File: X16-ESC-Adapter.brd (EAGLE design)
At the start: 101.6 x 41.2 mm, 0 parts

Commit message: Included the needed parts
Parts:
- added J1: CONN_1824750000, X16-ESC-Adapter:CONN3_1824750000_WED
- added U$1: CONN_BACKPLANE_ESC_ADAPTER, X16-ESC-Adapter:CONN_BACKPLANE_ESC_ADAPTER
- added U$2: CONN_JST_8_PIN, X16-ESC-Adapter:JST_8_PIN
- added U$3: LUMENIER, X16-ESC-Adapter:LUMENIER

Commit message: Curren tprogress on schem
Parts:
- removed J1: CONN_1824750000, X16-ESC-Adapter:CONN3_1824750000_WED
- removed U$2: CONN_JST_8_PIN, X16-ESC-Adapter:JST_8_PIN
- removed U$3: LUMENIER, X16-ESC-Adapter:LUMENIER
- added D1: GREEN, SparkFun-LED:LED-0603
- added ESC1, ESC2, ESC3, ESC4: CONN_1824750000, X16-ESC-Adapter:CONN3_1824750000_WED
- added LUMENIER_ESC_PORT: CONN_JST_8_PIN, X16-ESC-Adapter:JST_8_PIN
- added LUMINIER_ESC: LUMENIER, X16-ESC-Adapter:LUMENIER
- added RIZZ: 600, SparkFun-Resistors:0603
- renumbered U$1 to PWR
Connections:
- new net 12V: LUMINIER_ESC.VIN, PWR.12V@10, PWR.12V@11, PWR.12V@12, PWR.12V@3, PWR.12V@4, PWR.12V@5, PWR.12V@6, PWR.12V@7, PWR.12V@8, PWR.12V@9, RIZZ.1
- new net ESC1A: ESC1.1, ESC1.2, LUMINIER_ESC.1
- new net ESC1B: ESC1.3, ESC1.4, LUMINIER_ESC.2
- new net ESC1C: ESC1.5, ESC1.6, LUMINIER_ESC.3
- new net ESC2A: ESC2.1, ESC2.2, LUMINIER_ESC.4
- new net ESC2B: ESC2.3, ESC2.4, LUMINIER_ESC.5
- new net ESC2C: ESC2.5, ESC2.6, LUMINIER_ESC.6
- new net ESC3A: ESC3.5, ESC3.6, LUMINIER_ESC.9
- new net ESC3B: ESC3.3, ESC3.4, LUMINIER_ESC.8
- new net ESC3C: ESC3.1, ESC3.2, LUMINIER_ESC.7
- new net ESC4A: ESC4.5, ESC4.6, LUMINIER_ESC.12
- new net ESC4B: ESC4.3, ESC4.4, LUMINIER_ESC.11
- new net ESC4C: ESC4.1, ESC4.2, LUMINIER_ESC.10
- new net GND: D1.C, LUMENIER_ESC_PORT.2, LUMENIER_ESC_PORT.MECH1, LUMENIER_ESC_PORT.MECH2, LUMINIER_ESC.GND, PWR.GND@1, PWR.GND@10, PWR.GND@2, PWR.GND@3, PWR.GND@4, PWR.GND@5, PWR.GND@6, PWR.GND@7, PWR.GND@8, PWR.GND@9
- new net MTR_1: LUMENIER_ESC_PORT.5, PWR.PWM0
- new net MTR_2: LUMENIER_ESC_PORT.6, PWR.PWM1
- new net MTR_3: LUMENIER_ESC_PORT.7, PWR.PWM2
- new net MTR_4: LUMENIER_ESC_PORT.8, PWR.PWM3
- new net N$1: D1.A, RIZZ.2
- new net N$7: PWR.NC@1, PWR.NC@2, PWR.NC@3, PWR.NC@4, PWR.NC@5, PWR.NC@6
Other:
- board size 101.6 x 41.2 mm -> 101.6 x 41.1 mm

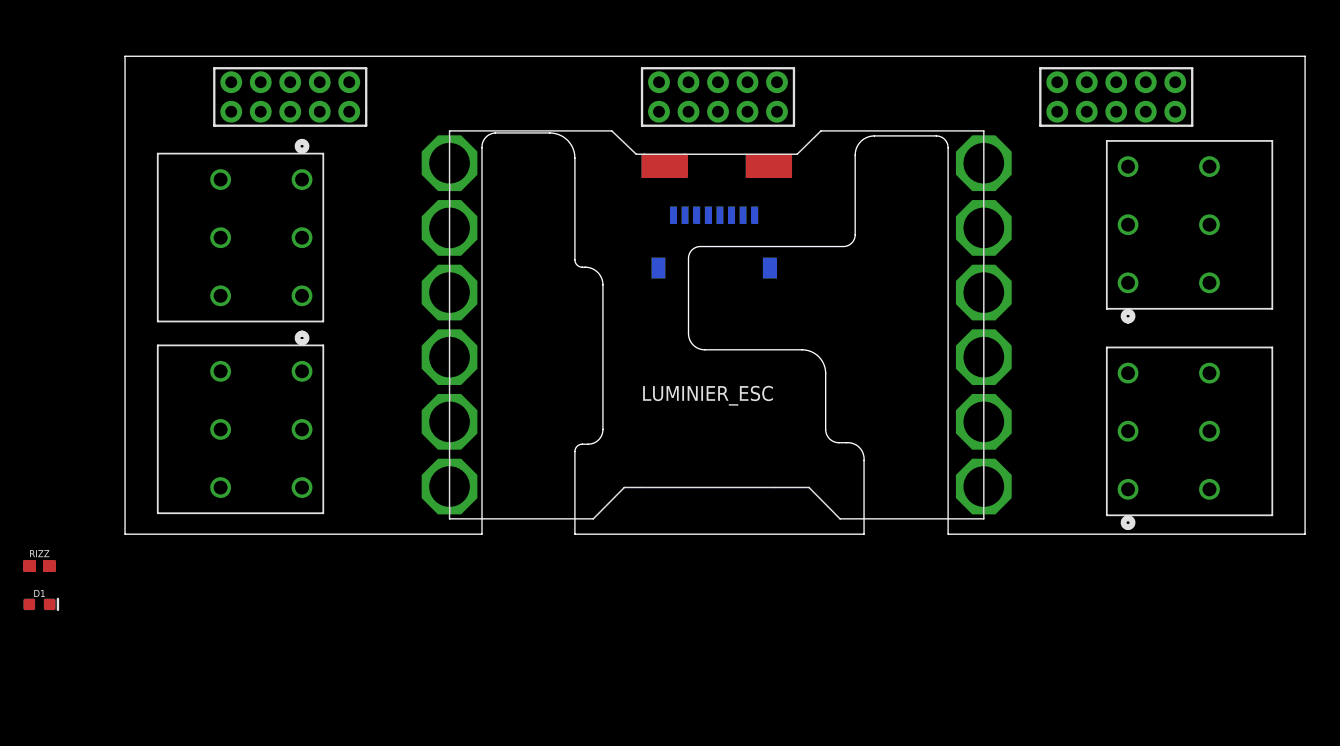
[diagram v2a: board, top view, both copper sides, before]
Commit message: Update X16-ESC-Adapter.brd
10/4/23 - Started Board Circuitry
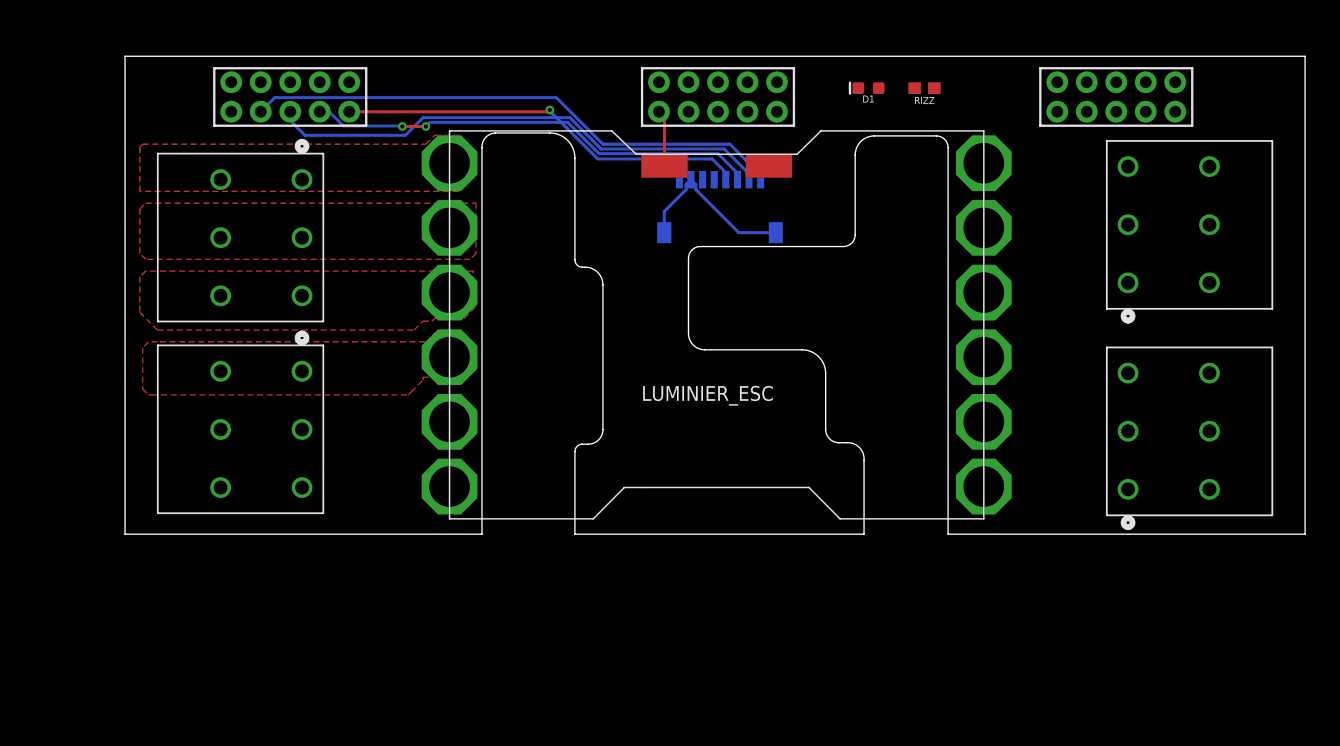
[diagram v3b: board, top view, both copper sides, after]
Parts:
- moved RIZZ 86.6 mm to (68.8, 38.4), turned to 180 degrees
- moved D1 84.1 mm to (64.0, 38.4), turned to 180 degrees
- moved LUMENIER_ESC_PORT 3.09 mm to (46.2, 29.7)
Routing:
- net MTR_4: track 0.00 -> 46.7 mm
- net MTR_3: track 0.00 -> 43.9 mm
- net MTR_2: track 0.00 -> 39.0 mm, vias 0 -> 2
- net MTR_1: track 0.00 -> 35.4 mm, vias 0 -> 1
- net GND: track 0.00 -> 22.6 mm
- added copper zone on layer 1, net ESC1A
- added copper zone on layer 1, net ESC1B
- added copper zone on layer 1, net ESC1C
- added copper zone on layer 1, net ESC2A
- added copper zone on layer 1, net N$2

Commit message: Update X16-ESC-Adapter.brd
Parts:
- moved RIZZ 4.83 mm to (64.0, 38.6)
- moved D1 3.31 mm to (60.7, 38.6)
- moved LUMENIER_ESC_PORT 0.76 mm to (46.2, 30.5)
- moved ESC3 0.51 mm to (86.4, 4.32)
- moved ESC1 0.51 mm to (15.2, 31.0)
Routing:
- net MTR_4: track 46.7 -> 51.3 mm
- net MTR_3: track 43.9 -> 48.3 mm
- net MTR_2: track 39.0 -> 42.2 mm
- net N$1: track 0.00 -> 1.58 mm
- net MTR_1: track 35.4 -> 36.1 mm, vias 1 -> 2
- net GND: track 22.6 -> 23.2 mm
- added copper zone on layer 1, net 12V
- added copper zone on layer 16, net ESC1A
- added copper zone on layer 16, net ESC1B
- added copper zone on layer 16, net ESC1C
- added copper zone on layer 16, net ESC2A
- added copper zone on layer 1, net ESC2B
- added copper zone on layer 16, net ESC2B
- added copper zone on layer 1, net ESC2C
- added copper zone on layer 16, net ESC2C
- added copper zone on layer 1, net ESC3A
- added copper zone on layer 16, net ESC3A
- added copper zone on layer 1, net ESC3B
- added copper zone on layer 16, net ESC3B
- added copper zone on layer 1, net ESC3C
- added copper zone on layer 16, net ESC3C
- added copper zone on layer 1, net ESC4A
- added copper zone on layer 16, net ESC4A
- added copper zone on layer 1, net ESC4B
- added copper zone on layer 16, net ESC4B
- added copper zone on layer 1, net ESC4C
- added copper zone on layer 16, net ESC4C
- added copper zone on layer 1, net GND
- removed copper zone on layer 1, net N$2

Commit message: Finished Layout
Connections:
- removed net N$7: PWR.NC@1, PWR.NC@2, PWR.NC@3, PWR.NC@4, PWR.NC@5, PWR.NC@6
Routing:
- net GND: track 23.2 -> 25.5 mm, vias 0 -> 1
- net MTR_3: track 48.3 -> 50.0 mm

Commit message: First set of changes after alumni design review
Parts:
- removed D1: GREEN, SparkFun-LED:LED-0603
- added HOPE: (no value), led:CHIPLED_0805
- moved LUMENIER_ESC_PORT 37.5 mm to (9.65, 38.6)
- moved RIZZ 3.57 mm to (67.6, 38.4)
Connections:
- net GND: now also HOPE.C; no longer D1.C
- net N$1: now also HOPE.A; no longer D1.A
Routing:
- net MTR_4: track 51.1 -> 0.00 mm
- net MTR_3: track 50.0 -> 0.00 mm
- net MTR_2: track 42.5 -> 0.00 mm, vias 2 -> 0
- net MTR_1: track 35.8 -> 0.00 mm, vias 2 -> 0
- net GND: track 25.5 -> 0.00 mm, vias 1 -> 0
- net N$1: track 1.58 -> 0.00 mm
- added copper zone on layer 16, net GND
- added copper zone on layer 1, net PWR
- removed copper zone on layer 1, net 12V
- removed copper zone on layer 1, net GND
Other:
- outline, holes or cut-outs redrawn

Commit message: Updated (11/4)
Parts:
- removed LUMENIER_ESC_PORT: CONN_JST_8_PIN, X16-ESC-Adapter:JST_8_PIN
- added J1: BM08B-SRSS-TB(LF)(SN), X16-ESC-Adapter:JST_BM08B-SRSS-TB(LF)(SN)
- moved RIZZ 0.72 mm to (68.1, 38.9)
- moved HOPE 0.72 mm to (62.7, 38.9)
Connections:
- net GND: now also J1.S1, J1.S2; no longer LUMENIER_ESC_PORT.2, LUMENIER_ESC_PORT.MECH1, LUMENIER_ESC_PORT.MECH2
- net MTR_1: now also J1.1; no longer LUMENIER_ESC_PORT.5
- net MTR_2: now also J1.2; no longer LUMENIER_ESC_PORT.6
- net MTR_3: now also J1.3; no longer LUMENIER_ESC_PORT.7
- net MTR_4: now also J1.4; no longer LUMENIER_ESC_PORT.8
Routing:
- net MTR_4: track 0.00 -> 20.7 mm
- net MTR_3: track 0.00 -> 16.4 mm
- net MTR_2: track 0.00 -> 11.8 mm
- net MTR_1: track 0.00 -> 6.69 mm
- net GND: track 0.00 -> 5.55 mm
- net N$1: track 0.00 -> 3.43 mm
- added copper zone on layer 1, net 12V
- added copper zone on layer 16, net 12V
- added copper zone on layer 1, net GND
- removed copper zone on layer 1, net PWR
